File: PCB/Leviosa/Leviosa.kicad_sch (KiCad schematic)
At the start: 32 parts, among them Q3 TIP122, Q4 TIP122, U1 LM324, U2 ATtiny13A-P, U3 TPS1H200AQDGNRQ1, U5 L7805, U6 SS495A

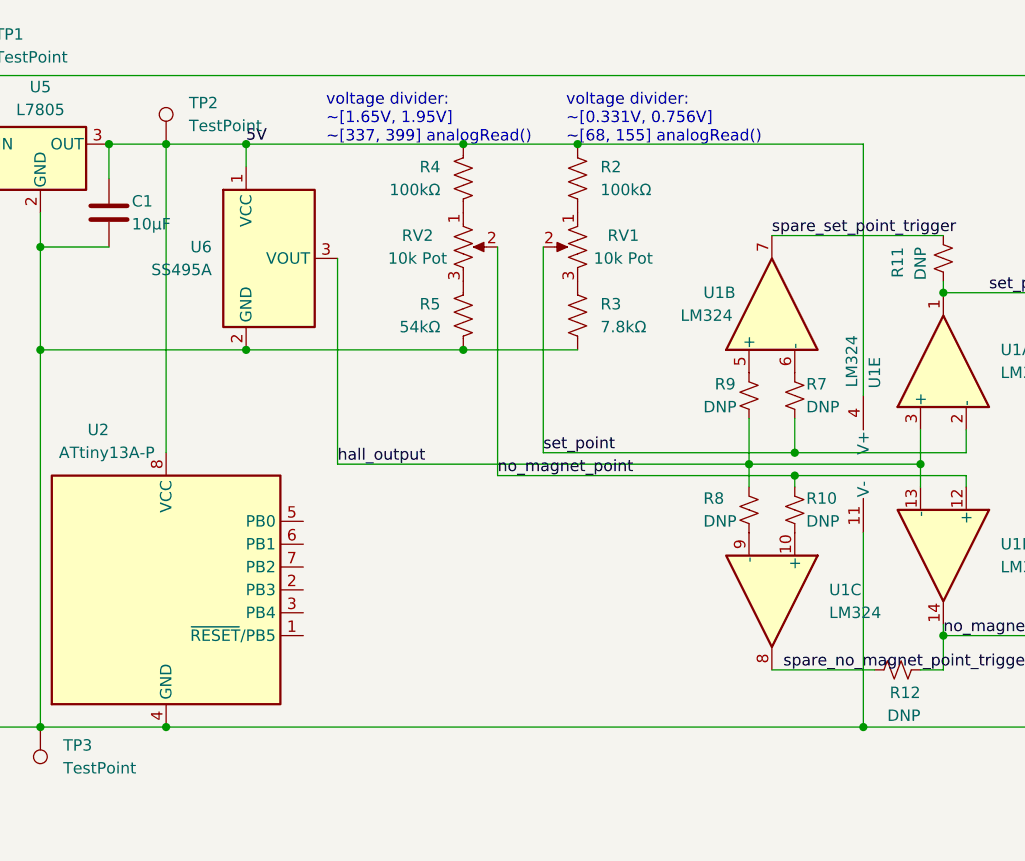
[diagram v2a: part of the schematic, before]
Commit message: add rough arduino wiring
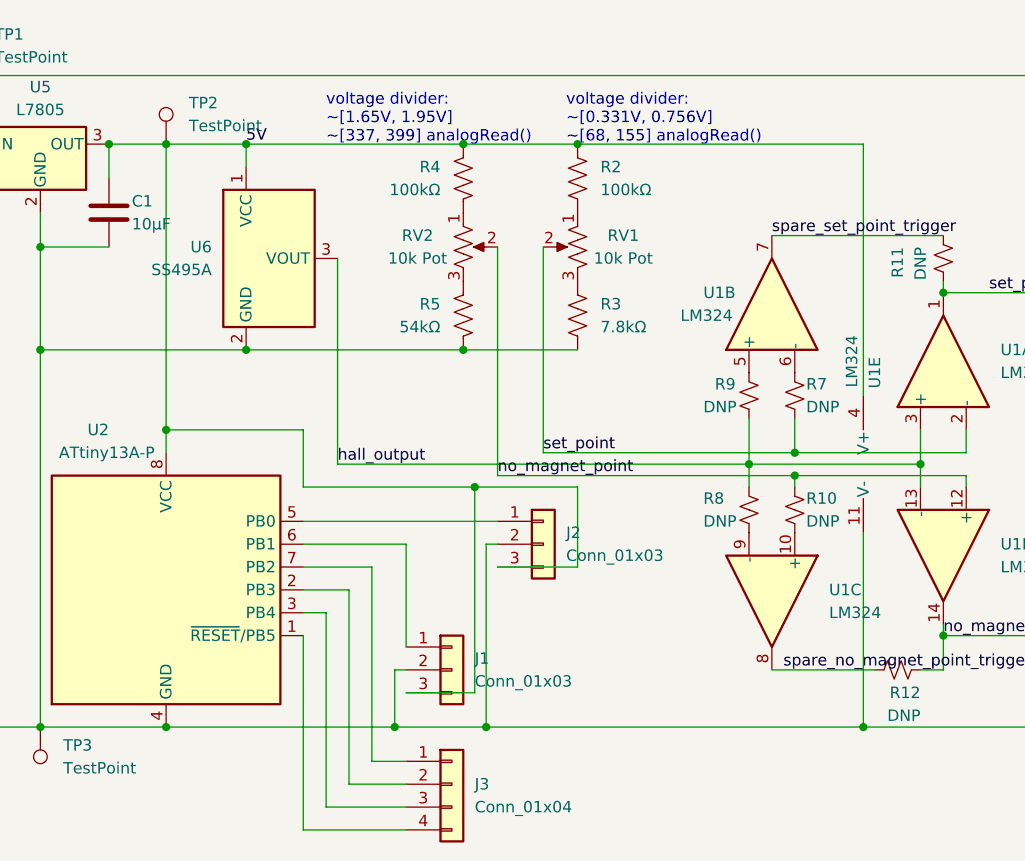
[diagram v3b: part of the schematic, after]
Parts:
- added J1, J2: Conn_01x03, symbol Connector_Generic:Conn_01x03
- added J3: Conn_01x04, symbol Connector_Generic:Conn_01x04
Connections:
- net 5V: now also J1.3 (Pin_3), J2.3 (Pin_3)
- net GND: now also J1.2 (Pin_2), J2.2 (Pin_2)
- net at U2.1 (~{RESET}/PB5): now also J3.4 (Pin_4)
- net at U2.2 (PB3): now also J3.2 (Pin_2)
- net at U2.3 (PB4): now also J3.3 (Pin_3)
- net at U2.5 (PB0): now also J2.1 (Pin_1)
- net at U2.6 (PB1): now also J1.1 (Pin_1)
- net at U2.7 (PB2): now also J3.1 (Pin_1)
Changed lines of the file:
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@@
     (rev "P1A")
   )
+  (junction (at 101.6 93.98) (diameter 0) (color 0 0 0 0)
+  )
   (junction (at 187.96 116.84) (diameter 0) (color 0 0 0 0)
   )
@@
   (junction (at 166.37 97.79) (diameter 0) (color 0 0 0 0)
   )
+  (junction (at 127 127) (diameter 0) (color 0 0 0 0)
+  )
   (junction (at 134.62 85.09) (diameter 0) (color 0 0 0 0)
   )
@@
   (junction (at 101.6 127) (diameter 0) (color 0 0 0 0)
   )
+  (junction (at 135.89 100.33) (diameter 0) (color 0 0 0 0)
+  )
   (junction (at 179.07 127) (diameter 0) (color 0 0 0 0)
   )
@@
   (junction (at 228.6 54.61) (diameter 0) (color 0 0 0 0)
   )
+  (junction (at 137.16 127) (diameter 0) (color 0 0 0 0)
+  )
   (junction (at 87.63 85.09) (diameter 0) (color 0 0 0 0)
   )
@@
     (stroke (width 0) (type default))
   )
+  (wire (pts (xy 138.43 109.22) (xy 147.32 109.22))
+    (stroke (width 0) (type default))
+  )
   (wire (pts (xy 187.96 78.74) (xy 213.36 78.74))
     (stroke (width 0) (type default))
   )
+  (wire (pts (xy 119.38 114.3) (xy 119.38 135.89))
+    (stroke (width 0) (type default))
+  )
+  (wire (pts (xy 147.32 100.33) (xy 135.89 100.33))
+    (stroke (width 0) (type default))
+  )
+  (wire (pts (xy 128.27 123.19) (xy 135.89 123.19))
+    (stroke (width 0) (type default))
+  )
+  (wire (pts (xy 101.6 93.98) (xy 101.6 96.52))
+    (stroke (width 0) (type default))
+  )
   (wire (pts (xy 87.63 127) (xy 101.6 127))
     (stroke (width 0) (type default))
@@
     (stroke (width 0) (type default))
   )
+  (wire (pts (xy 116.84 104.14) (xy 138.43 104.14))
+    (stroke (width 0) (type default))
+  )
   (wire (pts (xy 179.07 62.23) (xy 147.32 62.23))
     (stroke (width 0) (type default))
   )
+  (wire (pts (xy 121.92 133.35) (xy 128.27 133.35))
+    (stroke (width 0) (type default))
+  )
   (wire (pts (xy 80.01 54.61) (xy 228.6 54.61))
     (stroke (width 0) (type default))
@@
     (stroke (width 0) (type default))
   )
+  (wire (pts (xy 116.84 114.3) (xy 119.38 114.3))
+    (stroke (width 0) (type default))
+  )
+  (wire (pts (xy 116.84 106.68) (xy 128.27 106.68))
+    (stroke (width 0) (type default))
+  )
   (wire (pts (xy 228.6 62.23) (xy 251.46 62.23))
     (stroke (width 0) (type default))
@@
     (stroke (width 0) (type default))
   )
+  (wire (pts (xy 116.84 138.43) (xy 128.27 138.43))
+    (stroke (width 0) (type default))
+  )
   (wire (pts (xy 171.45 99.06) (xy 190.5 99.06))
     (stroke (width 0) (type default))
   )
+  (wire (pts (xy 121.92 111.76) (xy 121.92 133.35))
+    (stroke (width 0) (type default))
+  )
   (wire (pts (xy 25.4 68.58) (xy 25.4 71.12))
     (stroke (width 0) (type default))
@@
     (stroke (width 0) (type default))
   )
-  (wire (pts (xy 101.6 62.23) (xy 101.6 96.52))
+  (wire (pts (xy 101.6 62.23) (xy 101.6 93.98))
     (stroke (width 0) (type default))
   )
@@
     (stroke (width 0) (type default))
   )
+  (wire (pts (xy 128.27 106.68) (xy 128.27 118.11))
+    (stroke (width 0) (type default))
+  )
+  (wire (pts (xy 116.84 111.76) (xy 121.92 111.76))
+    (stroke (width 0) (type default))
+  )
   (wire (pts (xy 87.63 85.09) (xy 87.63 127))
     (stroke (width 0) (type default))
   )
+  (wire (pts (xy 147.32 109.22) (xy 147.32 100.33))
+    (stroke (width 0) (type default))
+  )
   (wire (pts (xy 25.4 105.41) (xy 60.96 105.41))
     (stroke (width 0) (type default))
@@
     (stroke (width 0) (type default))
   )
+  (wire (pts (xy 101.6 127) (xy 127 127))
+    (stroke (width 0) (type default))
+  )
   (wire (pts (xy 190.5 93.98) (xy 190.5 96.52))
     (stroke (width 0) (type default))
@@
     (stroke (width 0) (type default))
   )
+  (wire (pts (xy 116.84 93.98) (xy 101.6 93.98))
+    (stroke (width 0) (type default))
+  )
   (wire (pts (xy 187.96 116.84) (xy 213.36 116.84))
     (stroke (width 0) (type default))
@@
     (stroke (width 0) (type default))
   )
-  (wire (pts (xy 101.6 127) (xy 179.07 127))
-    (stroke (width 0) (type default))
-  )
   (wire (pts (xy 74.93 66.04) (xy 74.93 71.12))
     (stroke (width 0) (type default))
   )
+  (wire (pts (xy 116.84 109.22) (xy 124.46 109.22))
+    (stroke (width 0) (type default))
+  )
   (wire (pts (xy 68.58 63.5) (xy 68.58 59.69))
     (stroke (width 0) (type default))
@@
     (stroke (width 0) (type default))
   )
+  (wire (pts (xy 137.16 127) (xy 179.07 127))
+    (stroke (width 0) (type default))
+  )
   (wire (pts (xy 228.6 121.92) (xy 228.6 127))
     (stroke (width 0) (type default))
   )
+  (wire (pts (xy 116.84 100.33) (xy 116.84 93.98))
+    (stroke (width 0) (type default))
+  )
   (wire (pts (xy 171.45 96.52) (xy 190.5 96.52))
     (stroke (width 0) (type default))
@@
     (stroke (width 0) (type default))
   )
+  (wire (pts (xy 119.38 135.89) (xy 128.27 135.89))
+    (stroke (width 0) (type default))
+  )
+  (wire (pts (xy 127 127) (xy 137.16 127))
+    (stroke (width 0) (type default))
+  )
   (wire (pts (xy 187.96 120.65) (xy 187.96 116.84))
     (stroke (width 0) (type default))
@@
     (stroke (width 0) (type default))
   )
+  (wire (pts (xy 116.84 100.33) (xy 135.89 100.33))
+    (stroke (width 0) (type default))
+  )
+  (wire (pts (xy 135.89 123.19) (xy 135.89 100.33))
+    (stroke (width 0) (type default))
+  )
   (wire (pts (xy 179.07 62.23) (xy 179.07 90.17))
     (stroke (width 0) (type default))
   )
+  (wire (pts (xy 128.27 120.65) (xy 127 120.65))
+    (stroke (width 0) (type default))
+  )
   (wire (pts (xy 68.58 71.12) (xy 74.93 71.12))
     (stroke (width 0) (type default))
@@
     (stroke (width 0) (type default))
   )
+  (wire (pts (xy 124.46 130.81) (xy 128.27 130.81))
+    (stroke (width 0) (type default))
+  )
+  (wire (pts (xy 137.16 106.68) (xy 137.16 127))
+    (stroke (width 0) (type default))
+  )
+  (wire (pts (xy 124.46 109.22) (xy 124.46 130.81))
+    (stroke (width 0) (type default))
+  )
+  (wire (pts (xy 116.84 116.84) (xy 116.84 138.43))
+    (stroke (width 0) (type default))
+  )
   (wire (pts (xy 95.25 62.23) (xy 95.25 66.04))
     (stroke (width 0) (type default))
@@
     (stroke (width 0) (type default))
   )
+  (wire (pts (xy 127 120.65) (xy 127 127))
+    (stroke (width 0) (type default))
+  )
   (wire (pts (xy 74.93 127) (xy 87.63 127))
     (stroke (width 0) (type default))
   )
   (wire (pts (xy 190.5 100.33) (xy 190.5 99.06))
+    (stroke (width 0) (type default))
+  )
+  (wire (pts (xy 138.43 106.68) (xy 137.16 106.68))
     (stroke (width 0) (type default))
   )
@@
     )
   )
+  (symbol (lib_id "Connector_Generic:Conn_01x04") (at 133.35 133.35 0) (unit 1)
+    (in_bom yes) (on_board yes) (dnp no) (fields_autoplaced)
+    (property "Reference" "J3" (at 135.89 133.35 0)
+      (effects (font (size 1.27 1.27)) (justify left))
+    )
+    (property "Value" "Conn_01x04" (at 135.89 135.89 0)
+      (effects (font (size 1.27 1.27)) (justify left))
+    )
+    (property "Footprint" "" (at 133.35 133.35 0)
+      (effects (font (size 1.27 1.27)) hide)
+    )
+    (property "Datasheet" "~" (at 133.35 133.35 0)
+      (effects (font (size 1.27 1.27)) hide)
+    )
+    (pin "1")
+    (pin "2")
+    (pin "3")
+    (pin "4")
+    (instances
+      (project "Leviosa"
+        (path "/fe766911-203b-467c-b704-d4bd488f6c98"
+          (reference "J3") (unit 1)
+        )
+      )
+    )
+  )
   (symbol (lib_id "Device:D_Schottky") (at 228.6 58.42 270) (unit 1)
     (in_bom yes) (on_board yes) (dnp no) (fields_autoplaced)
@@
     )
   )
+  (symbol (lib_id "Connector_Generic:Conn_01x03") (at 143.51 106.68 0) (unit 1)
+    (in_bom yes) (on_board yes) (dnp no) (fields_autoplaced)
+    (property "Reference" "J2" (at 146.05 105.41 0)
+      (effects (font (size 1.27 1.27)) (justify left))
+    )
+    (property "Value" "Conn_01x03" (at 146.05 107.95 0)
+      (effects (font (size 1.27 1.27)) (justify left))
+    )
+    (property "Footprint" "" (at 143.51 106.68 0)
+      (effects (font (size 1.27 1.27)) hide)
+    )
+    (property "Datasheet" "~" (at 143.51 106.68 0)
+      (effects (font (size 1.27 1.27)) hide)
+    )
+    (pin "1")
+    (pin "2")
+    (pin "3")
+    (instances
+      (project "Leviosa"
+        (path "/fe766911-203b-467c-b704-d4bd488f6c98"
+          (reference "J2") (unit 1)
+        )
+      )
+    )
+  )
   (symbol (lib_id "Device:R_US") (at 134.62 81.28 0) (mirror x) (unit 1)
     (in_bom yes) (on_board yes) (dnp no)
@@
         )
       )
+    )
+  )
+  (symbol (lib_id "Connector_Generic:Conn_01x03") (at 133.35 120.65 0) (unit 1)
+    (in_bom yes) (on_board yes) (dnp no) (fields_autoplaced)
+    (property "Reference" "J1" (at 135.89 119.38 0)
+      (effects (font (size 1.27 1.27)) (justify left))
+    )
+    (property "Value" "Conn_01x03" (at 135.89 121.92 0)
+      (effects (font (size 1.27 1.27)) (justify left))
+    )
+    (property "Footprint" "" (at 133.35 120.65 0)
+      (effects (font (size 1.27 1.27)) hide)
+    )
+    (property "Datasheet" "~" (at 133.35 120.65 0)
+      (effects (font (size 1.27 1.27)) hide)
+    )
+    (pin "1")
+    (pin "2")
+    (pin "3")
+    (instances
+      (project "Leviosa"
+        (path "/fe766911-203b-467c-b704-d4bd488f6c98"
+          (reference "J1") (unit 1)
+        )
+      )

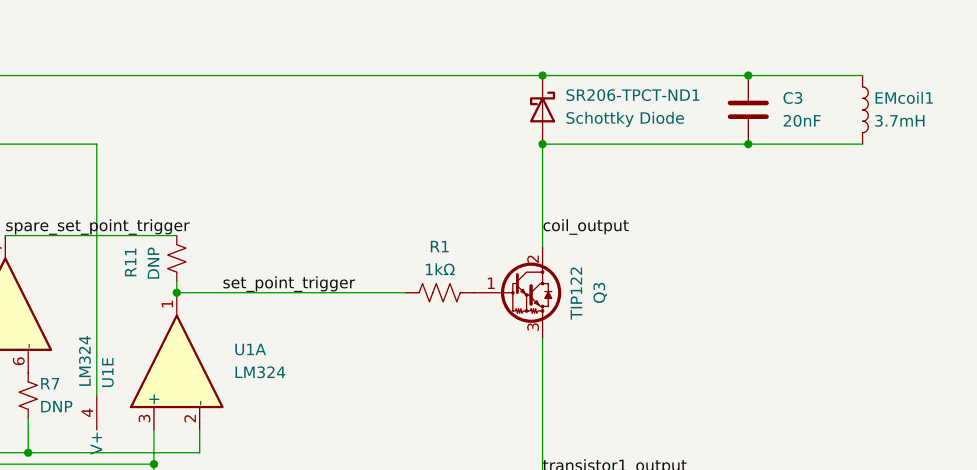
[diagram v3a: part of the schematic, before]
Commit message: Reviewed  PCB design and provided feedback. Updated the .gitignore as well
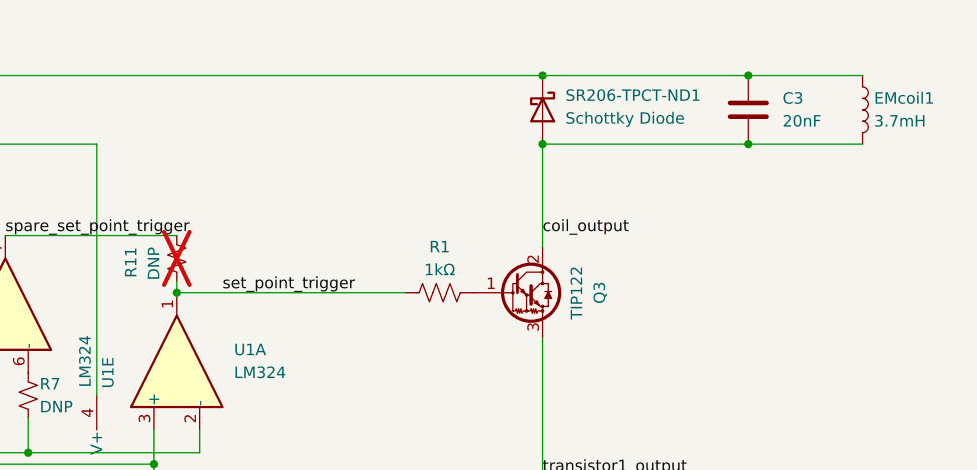
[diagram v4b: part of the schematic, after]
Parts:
- R11: now not fitted
